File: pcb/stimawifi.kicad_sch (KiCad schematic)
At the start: 14 parts, among them J1 Screw_Terminal_01x05, J2 Screw_Terminal_01x05, J3 Screw_Terminal_01x05, J4 Screw_Terminal_01x05, J5 Screw_Terminal_01x05, J8 Conn_01x02, U1 WEMOS_D1_mini

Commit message: Circuit diagram up to pcb
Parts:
- removed TP1: 5V, TestPoint:TestPoint_Pad_D1.5mm, symbol Connector:TestPoint
- removed TP2: 3v3, TestPoint:TestPoint_Pad_D1.5mm, symbol Connector:TestPoint
- removed TP3: GND, TestPoint:TestPoint_Pad_D1.5mm, symbol Connector:TestPoint
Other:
- moved on the sheet: H1, H2, H3, H4, J1, J4, J5, J8, U1

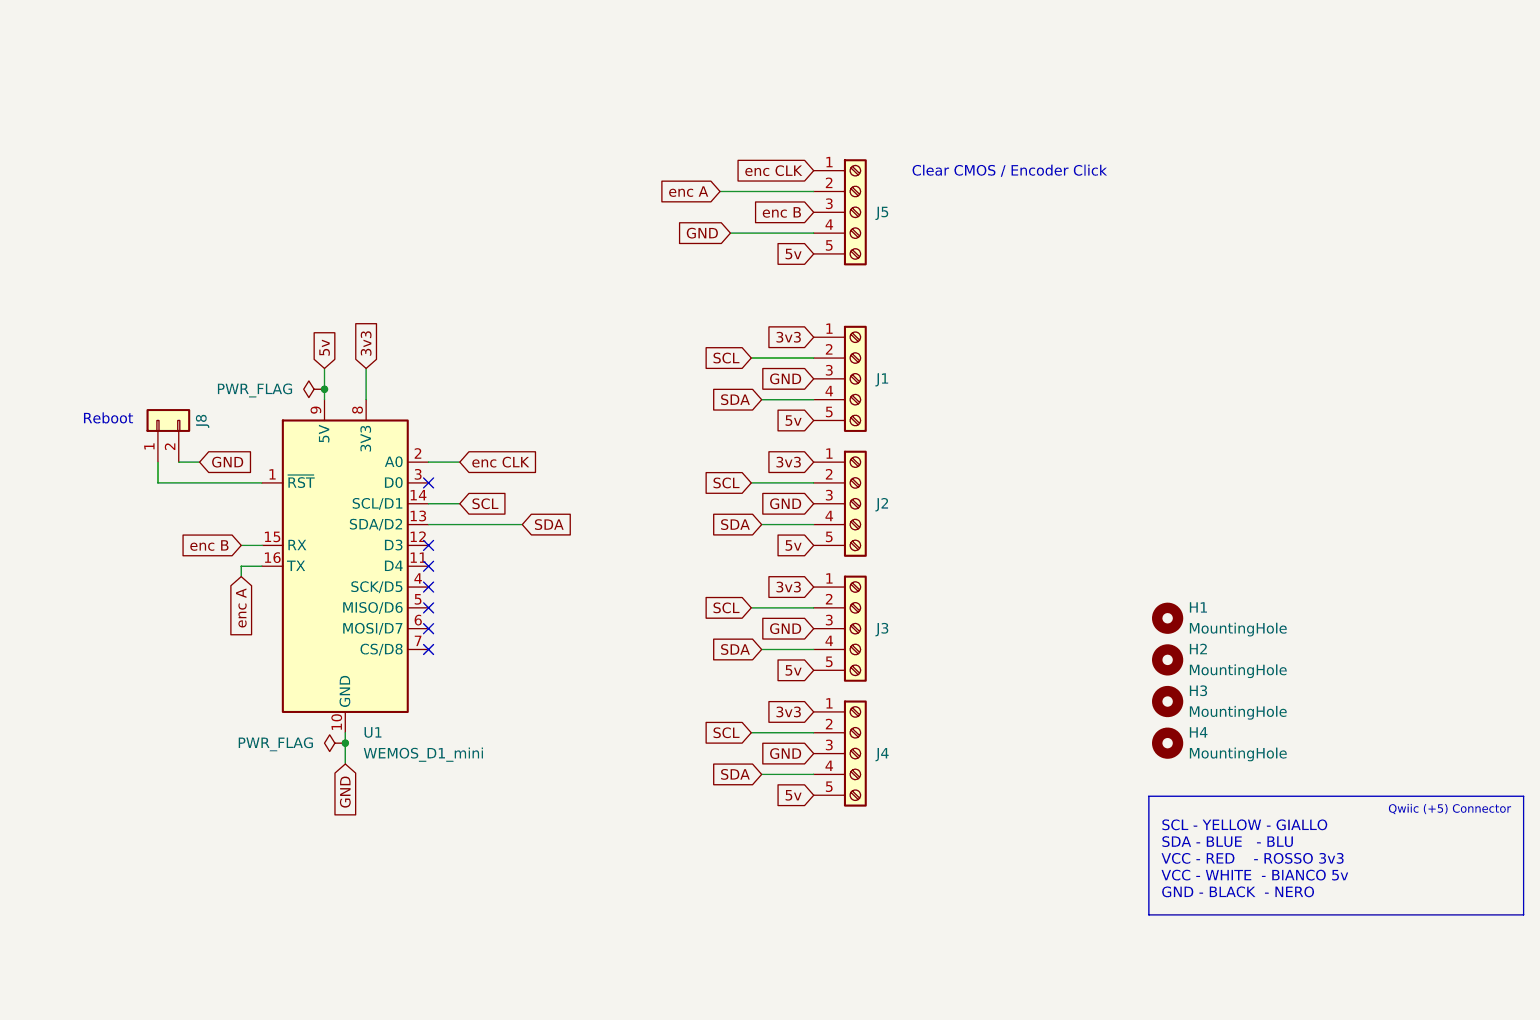
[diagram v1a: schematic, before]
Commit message: Migrated symbols, footprint and 3d models to local libraries
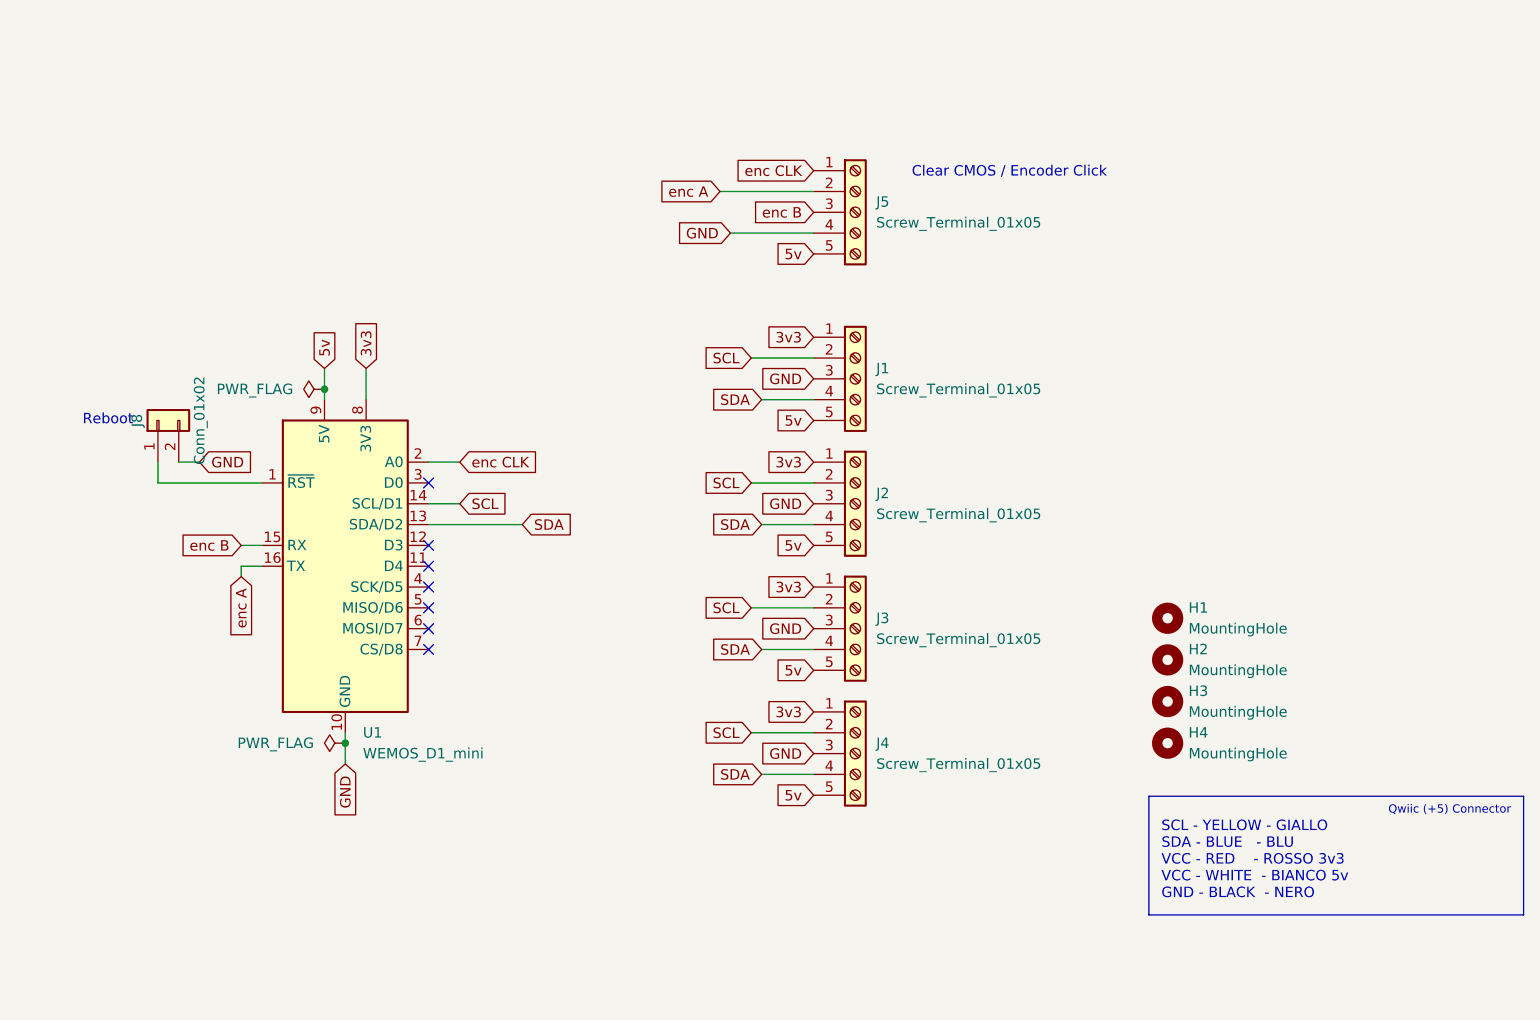
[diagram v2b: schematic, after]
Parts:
- H1, H2, H3, H4: footprint MountingHole:MountingHole_3.2mm_M3 -> Stima.Library:MountingHole_3.2mm_M3; symbol Mechanical:MountingHole -> Stima:MountingHole
- J1, J2, J3, J4, J5: footprint TerminalBlock:TerminalBlock_Xinya_XY308-2.54-5P_1x05_P2.54mm_Horizontal -> Stima.Library:TerminalBlock_Xinya_XY308-2.54-5P_1x05_P2.54mm_Horizontal; symbol Connector:Screw_Terminal_01x05 -> Stima:Screw_Terminal_01x05
- J8: footprint Connector_PinHeader_2.54mm:PinHeader_1x02_P2.54mm_Vertical -> Stima.Library:PinHeader_1x02_P2.54mm_Vertical; symbol Connector_Generic:Conn_01x02 -> Stima:Conn_01x02
- U1: footprint RF_Module:WEMOS_D1_mini_light -> Stima.Library:WEMOS_D1_mini_light; symbol RF_Module:WEMOS_D1_mini -> Stima:WEMOS_D1_mini
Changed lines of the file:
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@@
 	)
 	(symbol
-		(lib_id "Mechanical:MountingHole")
+		(lib_id "Stima:MountingHole")
 		(at 179.07 132.08 0)
 		(unit 1)
@@
 			)
 		)
-		(property "Footprint" "MountingHole:MountingHole_3.2mm_M3"
+		(property "Footprint" "Stima.Library:MountingHole_3.2mm_M3"
 			(at 179.07 132.08 0)
 			(effects
@@
 	)
 	(symbol
-		(lib_id "Connector:Screw_Terminal_01x05")
+		(lib_id "Stima:Screw_Terminal_01x05")
 		(at 140.97 77.47 0)
 		(unit 1)
@@
 		(fields_autoplaced yes)
 		(property "Reference" "J5"
-			(at 143.51 77.4699 0)
+			(at 143.51 76.1999 0)
 			(effects
 				(font
@@
 		)
 		(property "Value" "Screw_Terminal_01x05"
-			(at 147.32 77.47 90)
-			(effects
-				(font
-					(size 1.27 1.27)
-				)
-				(hide yes)
-			)
-		)
-		(property "Footprint" "TerminalBlock:TerminalBlock_Xinya_XY308-2.54-5P_1x05_P2.54mm_Horizontal"
+			(at 143.51 78.7399 0)
+			(effects
+				(font
+					(size 1.27 1.27)
+				)
+				(justify left)
+			)
+		)
+		(property "Footprint" "Stima.Library:TerminalBlock_Xinya_XY308-2.54-5P_1x05_P2.54mm_Horizontal"
 			(at 140.97 77.47 0)
 			(effects
@@
 	)
 	(symbol
-		(lib_id "Mechanical:MountingHole")
+		(lib_id "Stima:MountingHole")
 		(at 179.07 127 0)
 		(unit 1)
@@
 			)
 		)
-		(property "Footprint" "MountingHole:MountingHole_3.2mm_M3"
+		(property "Footprint" "Stima.Library:MountingHole_3.2mm_M3"
 			(at 179.07 127 0)
 			(effects
@@
 	)
 	(symbol
-		(lib_id "Connector:Screw_Terminal_01x05")
+		(lib_id "Stima:Screw_Terminal_01x05")
 		(at 140.97 143.51 0)
 		(unit 1)
@@
 		(fields_autoplaced yes)
 		(property "Reference" "J4"
-			(at 143.51 143.5099 0)
+			(at 143.51 142.2399 0)
 			(effects
 				(font
@@
 		)
 		(property "Value" "Screw_Terminal_01x05"
-			(at 147.32 143.51 90)
-			(effects
-				(font
-					(size 1.27 1.27)
-				)
-				(hide yes)
-			)
-		)
-		(property "Footprint" "TerminalBlock:TerminalBlock_Xinya_XY308-2.54-5P_1x05_P2.54mm_Horizontal"
+			(at 143.51 144.7799 0)
+			(effects
+				(font
+					(size 1.27 1.27)
+				)
+				(justify left)
+			)
+		)
+		(property "Footprint" "Stima.Library:TerminalBlock_Xinya_XY308-2.54-5P_1x05_P2.54mm_Horizontal"
 			(at 140.97 143.51 0)
 			(effects
@@
 	)
 	(symbol
-		(lib_id "Connector:Screw_Terminal_01x05")
+		(lib_id "Stima:Screw_Terminal_01x05")
 		(at 140.97 128.27 0)
 		(unit 1)
@@
 		(fields_autoplaced yes)
 		(property "Reference" "J3"
-			(at 143.51 128.2699 0)
+			(at 143.51 126.9999 0)
 			(effects
 				(font
@@
 		)
 		(property "Value" "Screw_Terminal_01x05"
-			(at 147.32 128.27 90)
-			(effects
-				(font
-					(size 1.27 1.27)
-				)
-				(hide yes)
-			)
-		)
-		(property "Footprint" "TerminalBlock:TerminalBlock_Xinya_XY308-2.54-5P_1x05_P2.54mm_Horizontal"
+			(at 143.51 129.5399 0)
+			(effects
+				(font
+					(size 1.27 1.27)
+				)
+				(justify left)
+			)
+		)
+		(property "Footprint" "Stima.Library:TerminalBlock_Xinya_XY308-2.54-5P_1x05_P2.54mm_Horizontal"
 			(at 140.97 128.27 0)
 			(effects
@@
 	)
 	(symbol
-		(lib_id "Connector:Screw_Terminal_01x05")
+		(lib_id "Stima:Screw_Terminal_01x05")
 		(at 140.97 113.03 0)
 		(unit 1)
@@
 		(fields_autoplaced yes)
 		(property "Reference" "J2"
-			(at 143.51 113.0299 0)
+			(at 143.51 111.7599 0)
 			(effects
 				(font
@@
 		)
 		(property "Value" "Screw_Terminal_01x05"
-			(at 147.32 113.03 90)
-			(effects
-				(font
-					(size 1.27 1.27)
-				)
-				(hide yes)
-			)
-		)
-		(property "Footprint" "TerminalBlock:TerminalBlock_Xinya_XY308-2.54-5P_1x05_P2.54mm_Horizontal"
+			(at 143.51 114.2999 0)
+			(effects
+				(font
+					(size 1.27 1.27)
+				)
+				(justify left)
+			)
+		)
+		(property "Footprint" "Stima.Library:TerminalBlock_Xinya_XY308-2.54-5P_1x05_P2.54mm_Horizontal"
 			(at 140.97 113.03 0)
 			(effects
@@
 	)
 	(symbol
-		(lib_id "RF_Module:WEMOS_D1_mini")
+		(lib_id "Stima:WEMOS_D1_mini")
 		(at 78.74 120.65 0)
 		(unit 1)
@@
 		(fields_autoplaced yes)
 		(property "Reference" "U1"
-			(at 80.9341 140.97 0)
+			(at 80.8833 140.97 0)
 			(effects
 				(font
@@
 		)
 		(property "Value" "WEMOS_D1_mini"
-			(at 80.9341 143.51 0)
-			(effects
-				(font
-					(size 1.27 1.27)
-				)
-				(justify left)
-			)
-		)
-		(property "Footprint" "RF_Module:WEMOS_D1_mini_light"
+			(at 80.8833 143.51 0)
+			(effects
+				(font
+					(size 1.27 1.27)
+				)
+				(justify left)
+			)
+		)
+		(property "Footprint" "Stima.Library:WEMOS_D1_mini_light"
 			(at 78.74 149.86 0)
 			(effects
@@
 	)
 	(symbol
-		(lib_id "Connector_Generic:Conn_01x02")
+		(lib_id "Stima:Conn_01x02")
 		(at 55.88 102.87 90)
 		(unit 1)
@@
 		(dnp no)
 		(property "Reference" "J8"
-			(at 61.214 102.87 0)
+			(at 53.34 102.87 0)
 			(effects
 				(font
@@
 		)
 		(property "Value" "Conn_01x02"
-			(at 62.23 102.87 0)
-			(effects
-				(font
-					(size 1.27 1.27)
-				)
-				(hide yes)
-			)
-		)
-		(property "Footprint" "Connector_PinHeader_2.54mm:PinHeader_1x02_P2.54mm_Vertical"
+			(at 60.96 102.87 0)
+			(effects
+				(font
+					(size 1.27 1.27)
+				)
+			)
+		)
+		(property "Footprint" "Stima.Library:PinHeader_1x02_P2.54mm_Vertical"
 			(at 55.88 102.87 0)
 			(effects
@@
 	)
 	(symbol
-		(lib_id "Mechanical:MountingHole")
+		(lib_id "Stima:MountingHole")
 		(at 179.07 142.24 0)
 		(unit 1)
@@
 			)
 		)
-		(property "Footprint" "MountingHole:MountingHole_3.2mm_M3"
+		(property "Footprint" "Stima.Library:MountingHole_3.2mm_M3"
 			(at 179.07 142.24 0)
 			(effects
@@
 	)
 	(symbol
-		(lib_id "Connector:Screw_Terminal_01x05")
+		(lib_id "Stima:Screw_Terminal_01x05")
 		(at 140.97 97.79 0)
 		(unit 1)
@@
 		(fields_autoplaced yes)
 		(property "Reference" "J1"
-			(at 143.51 97.7899 0)
+			(at 143.51 96.5199 0)
 			(effects
 				(font
@@
 		)
 		(property "Value" "Screw_Terminal_01x05"
-			(at 147.32 97.79 90)
-			(effects
-				(font
-					(size 1.27 1.27)
-				)
-				(hide yes)
-			)
-		)
-		(property "Footprint" "TerminalBlock:TerminalBlock_Xinya_XY308-2.54-5P_1x05_P2.54mm_Horizontal"
+			(at 143.51 99.0599 0)
+			(effects
+				(font
+					(size 1.27 1.27)
+				)
+				(justify left)
+			)
+		)
+		(property "Footprint" "Stima.Library:TerminalBlock_Xinya_XY308-2.54-5P_1x05_P2.54mm_Horizontal"
 			(at 140.97 97.79 0)
 			(effects
@@
 	)
 	(symbol
-		(lib_id "Mechanical:MountingHole")
+		(lib_id "Stima:MountingHole")
 		(at 179.07 137.16 0)
 		(unit 1)
@@
 			)
 		)
-		(property "Footprint" "MountingHole:MountingHole_3.2mm_M3"
+		(property "Footprint" "Stima.Library:MountingHole_3.2mm_M3"
 			(at 179.07 137.16 0)
 			(effects
